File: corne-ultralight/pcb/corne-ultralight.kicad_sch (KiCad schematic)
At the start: 102 parts, among them J2 OLED, J7 OLED, SW1 SW_PUSH, SW10 SW_PUSH, SW11 SW_PUSH, SW12 SW_PUSH, SW13 SW_PUSH, SW14 SW_PUSH, SW15 SW_PUSH, SW16 SW_PUSH, SW17 SW_PUSH, SW18 SW_PUSH, SW19 SW_PUSH, SW2 SW_PUSH, SW20 SW_PUSH, SW21 SW_PUSH, SW22 SW_PUSH, SW23 SW_PUSH, SW24 SW_PUSH, SW25 SW_PUSH, SW26 SW_PUSH, SW27 SW_PUSH, SW28 SW_PUSH, SW29 SW_PUSH, SW3 SW_PUSH, SW30 SW_PUSH, SW31 SW_PUSH, SW32 SW_PUSH, SW33 SW_PUSH, SW34 SW_PUSH, SW35 SW_PUSH, SW36 SW_PUSH, SW37 SW_PUSH, SW38 SW_PUSH, SW39 SW_PUSH, SW4 SW_PUSH, SW40 SW_PUSH, SW41 SW_PUSH, SW42 SW_PUSH, SW5 SW_PUSH, SW6 SW_PUSH, SW7 SW_PUSH, SW8 SW_PUSH, SW9 SW_PUSH, U1 ProMicro, U2 ProMicro

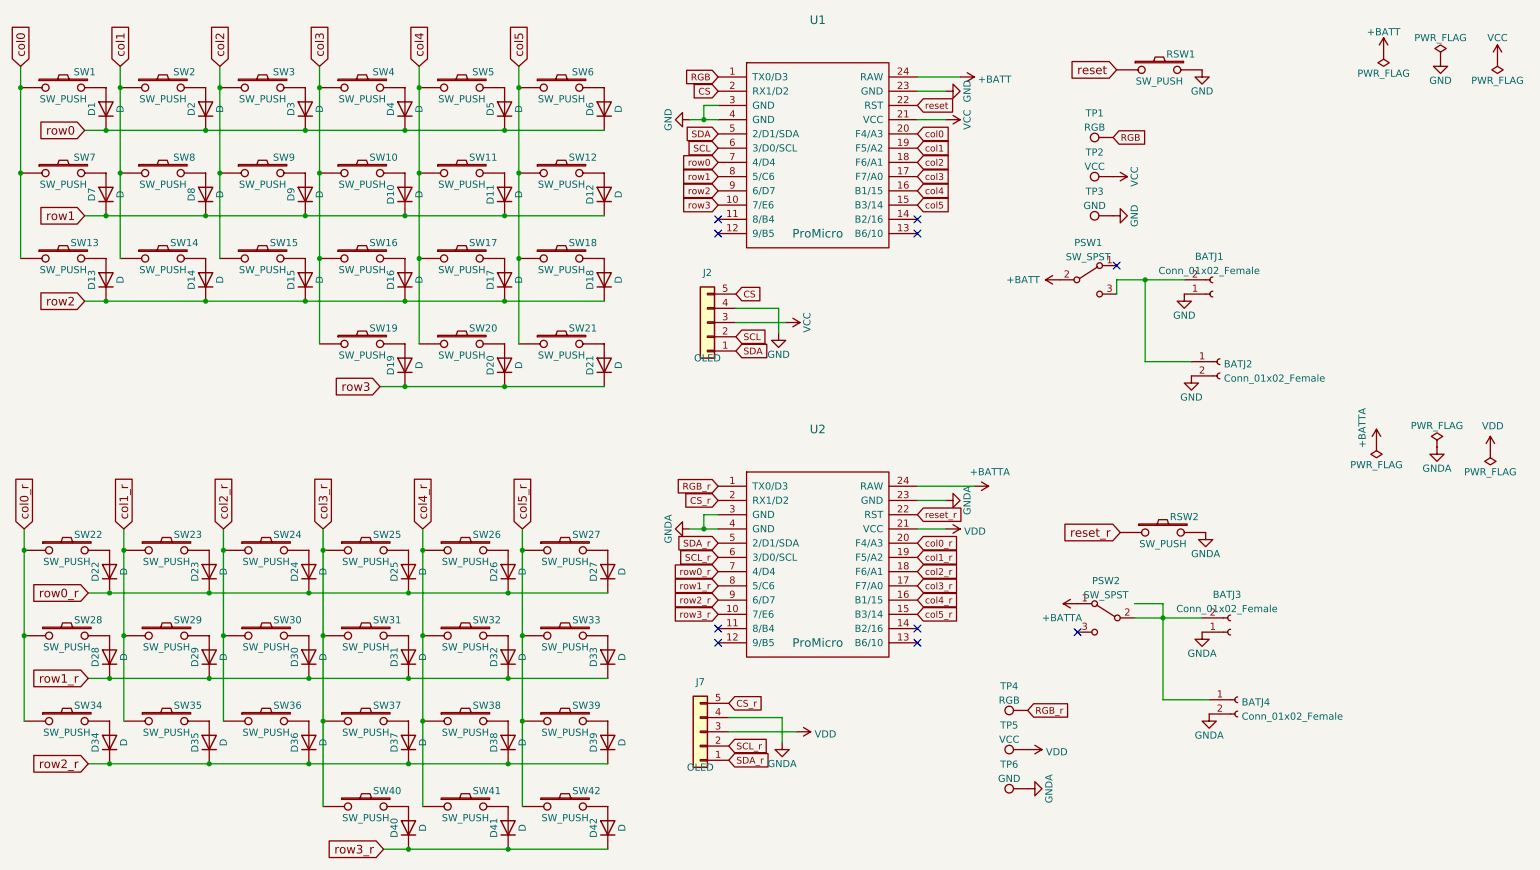
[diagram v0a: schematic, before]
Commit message: modify ultralight with kailh hotswap
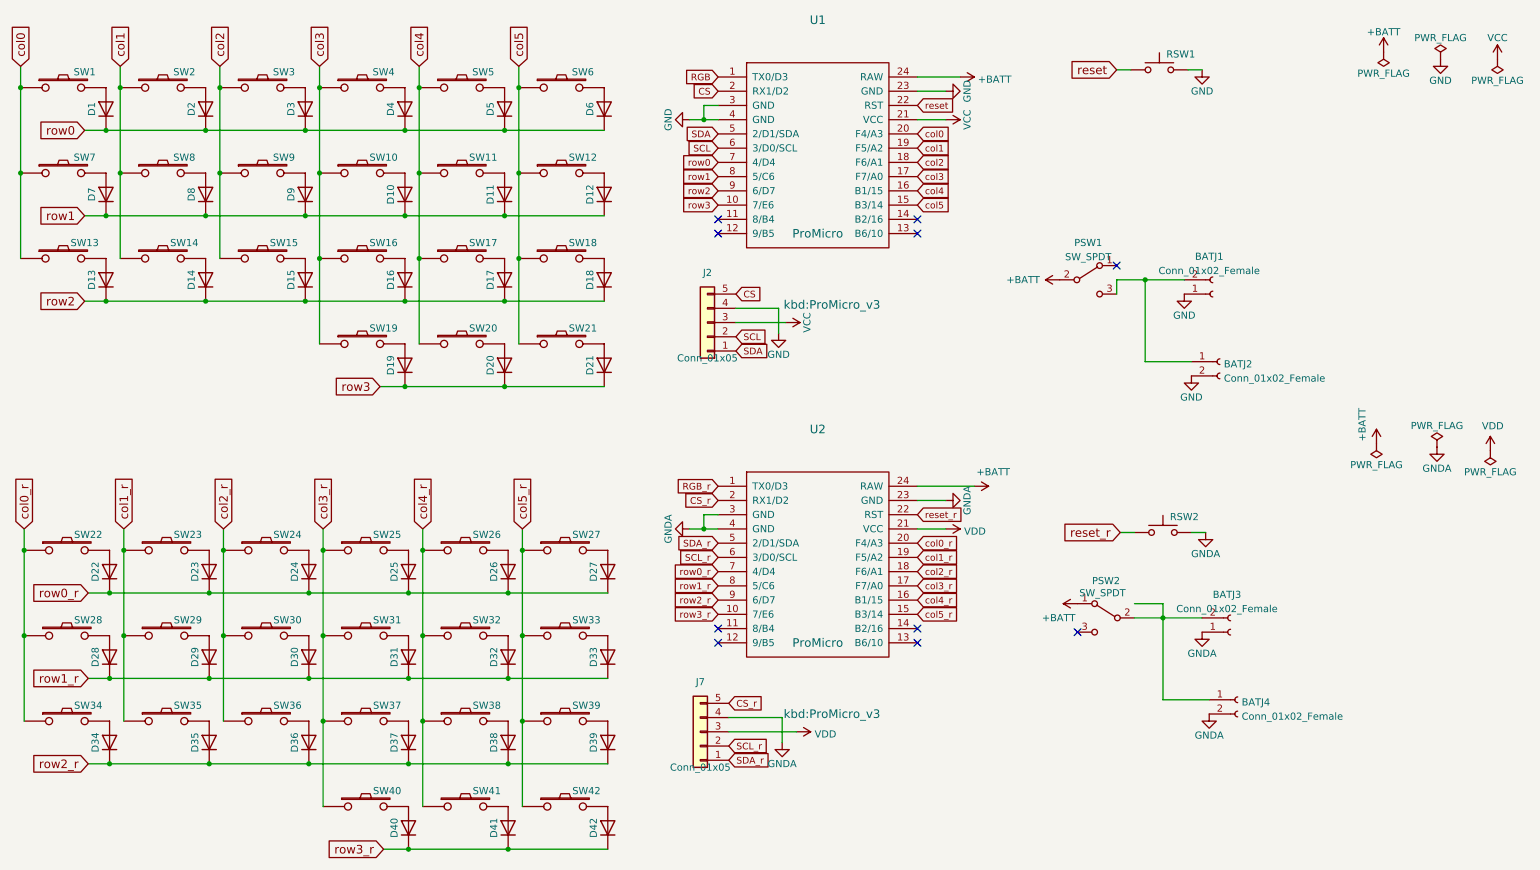
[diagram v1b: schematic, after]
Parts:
- removed TP1, TP4: RGB, TestPoint:TestPoint_Pad_D1.5mm, symbol Connector:TestPoint
- removed TP2, TP5: VCC, TestPoint:TestPoint_Pad_D1.5mm, symbol Connector:TestPoint
- removed TP3, TP6: GND, TestPoint:TestPoint_Pad_D1.5mm, symbol Connector:TestPoint
- BATJ1, BATJ2, BATJ3, BATJ4, U1, U2: now left out of the parts list
- D1, D10, D11, D12, D13, D14, D15, D16, D17, D18, D19, D2, D20, D21, D22, D23, D24, D25, D26, D27, D28, D29, D3, D30, D31, D32, D33, D34, D35, D36, D37, D38, D39, D4, D40, D41, D42, D5, D6, D7, D8, D9: value D -> 0805 1n4148 SOD-123; symbol Device:D -> kbd:D; JLC (none) -> 0805; LCSC (none) -> C444720
- J2, J7: value OLED -> Conn_01x05; now left out of the parts list
- PSW1, PSW2: value SW_SPST -> SW_SPDT; now left out of the parts list
- RSW1, RSW2: value SW_PUSH -> SW_Push_Reset; symbol kbd:SW_PUSH -> kbd:SW_Push_Reset; LCSC (none) -> C5333465; now left out of the parts list
- SW1, SW10, SW11, SW12, SW13, SW14, SW15, SW16, SW17, SW18, SW19, SW2, SW20, SW22, SW23, SW24, SW25, SW26, SW27, SW28, SW29, SW3, SW30, SW31, SW32, SW33, SW34, SW35, SW36, SW37, SW38, SW39, SW4, SW40, SW41, SW5, SW6, SW7, SW8, SW9: value SW_PUSH -> Kailh PG1350; footprint gateron-ks27:gateron-ks27-choc-v1 -> kbd:ChocV1_V2_Hotswap; LCSC (none) -> C5333465
- SW21, SW42: value SW_PUSH -> Kailh PG1350; footprint gateron-ks27:gateron-ks27-choc-v1-1.5u -> kbd:ChocV1_V2_Hotswap_1.5u; symbol kbd:SW_PUSH -> kbd:SW_PUSH_1.5; LCSC (none) -> C5333465
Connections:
- net +BATTA is gone; now on net +BATT: PSW2.1 (A), U2.24 (RAW)
